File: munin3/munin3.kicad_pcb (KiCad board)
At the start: 2 copper layers, 100 x 100 mm, 83 parts, among them J1 Conn_Coaxial, J2 Conn_Coaxial, J3 Conn_01x02_Male, J4 Conn_01x02_Male, T1 Q_NMOS_DSG, T2 Q_NMOS_DSG, T3 BSS84, T4 BST82, U1 MC78L08_SO8, U2 LMC6482

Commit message: Fixed drain connection, fixed final xfmr connection
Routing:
- net Net-(C10-Pad2): track 0.00 -> 23.2 mm
- net Net-(C10-Pad1): track 0.00 -> 16.2 mm
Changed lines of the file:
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@@
     (thickness 1.6)
     (drawings 12)
-    (tracks 543)
+    (tracks 555)
     (zones 0)
     (modules 83)
@@
   (layers
     (0 F.Cu signal)
-    (31 B.Cu signal)
+    (31 B.Cu signal hide)
     (32 B.Adhes user)
     (33 F.Adhes user)
@@
   (segment (start 102.101 82.243) (end 104.6475 82.243) (width 0.4) (layer F.Cu) (net 2))
   (segment (start 104.6475 82.243) (end 104.765 82.1255) (width 0.4) (layer F.Cu) (net 2))
+  (segment (start 160.986 82.659) (end 156.008 82.659) (width 0.4) (layer F.Cu) (net 3))
+  (segment (start 156.008 82.659) (end 154.694 81.345) (width 0.4) (layer F.Cu) (net 3))
+  (segment (start 154.694 81.345) (end 147.572 81.345) (width 4) (layer F.Cu) (net 3))
+  (segment (start 147.572 81.345) (end 146.002 79.775) (width 0.4) (layer F.Cu) (net 3))
   (segment (start 106.04 127.04) (end 108.58 124.5) (width 0.4) (layer B.Cu) (net 4))
   (segment (start 105.669 88.77) (end 108.4036 86.0354) (width 0.4) (layer F.Cu) (net 4))
@@
   (segment (start 109.05 89.55) (end 109.074 89.55) (width 0.4) (layer F.Cu) (net 6))
   (via (at 109.05 89.55) (size 0.8) (drill 0.4) (layers F.Cu B.Cu) (net 6))
+  (segment (start 160.986 103.659) (end 156.54 103.659) (width 0.4) (layer F.Cu) (net 7))
+  (segment (start 156.54 103.659) (end 155.638 104.561) (width 0.4) (layer F.Cu) (net 7))
+  (segment (start 147.408 104.561) (end 146.212 105.757) (width 0.4) (layer F.Cu) (net 7))
+  (segment (start 160.986 103.659) (end 159.84 103.659) (width 0.4) (layer F.Cu) (net 7))
+  (segment (start 159.84 103.659) (end 157.263 101.082) (width 0.4) (layer F.Cu) (net 7))
+  (segment (start 157.263 101.082) (end 154.464 101.082) (width 0.4) (layer F.Cu) (net 7))
+  (segment (start 155.638 104.561) (end 150.985 104.561) (width 4) (layer F.Cu) (net 7))
+  (segment (start 150.985 104.561) (end 147.408 104.561) (width 4) (layer F.Cu) (net 7))
   (segment (start 110.609 99.675) (end 110.609 103.302) (width 0.4) (layer F.Cu) (net 8))
   (segment (start 112.455 97.823) (end 110.609 99.669) (width 0.4) (layer F.Cu) (net 8))

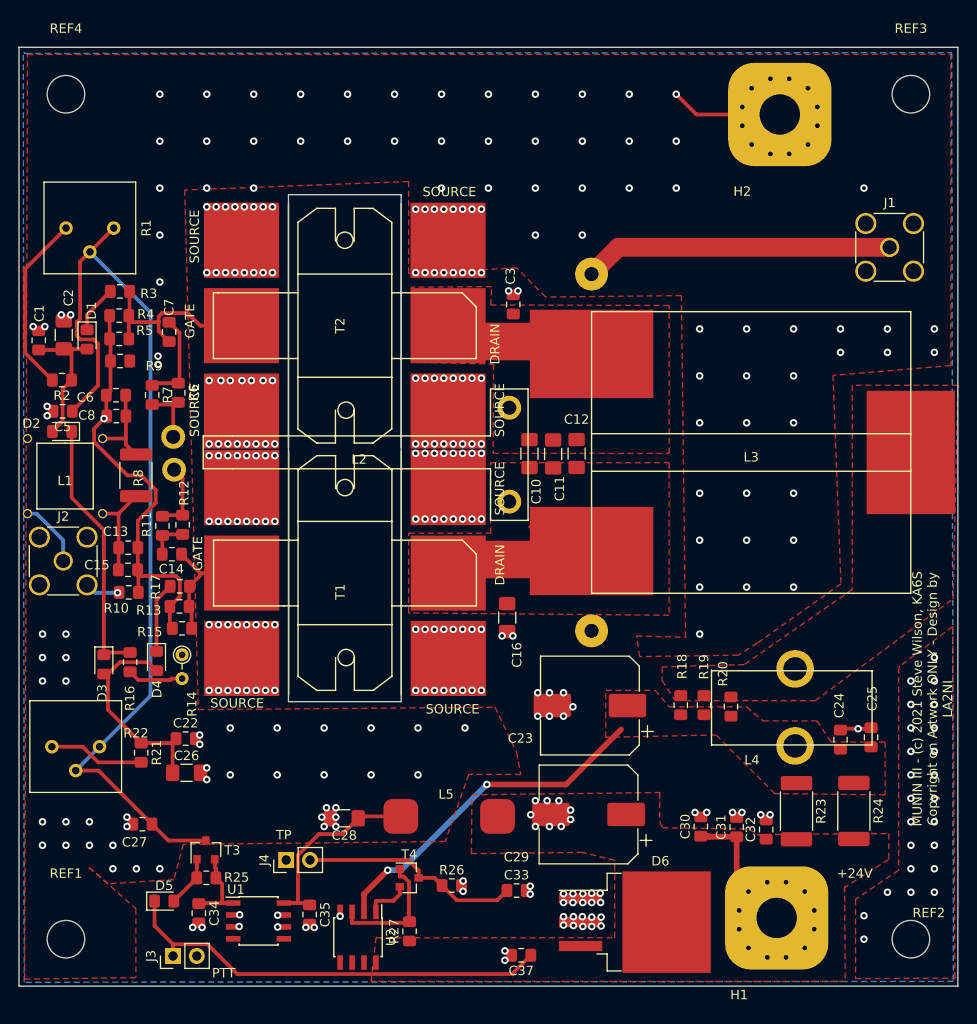
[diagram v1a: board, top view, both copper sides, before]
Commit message: Removed short between C8 and C15 on schem. Beefed up power/ground/Power Xfmr connections.
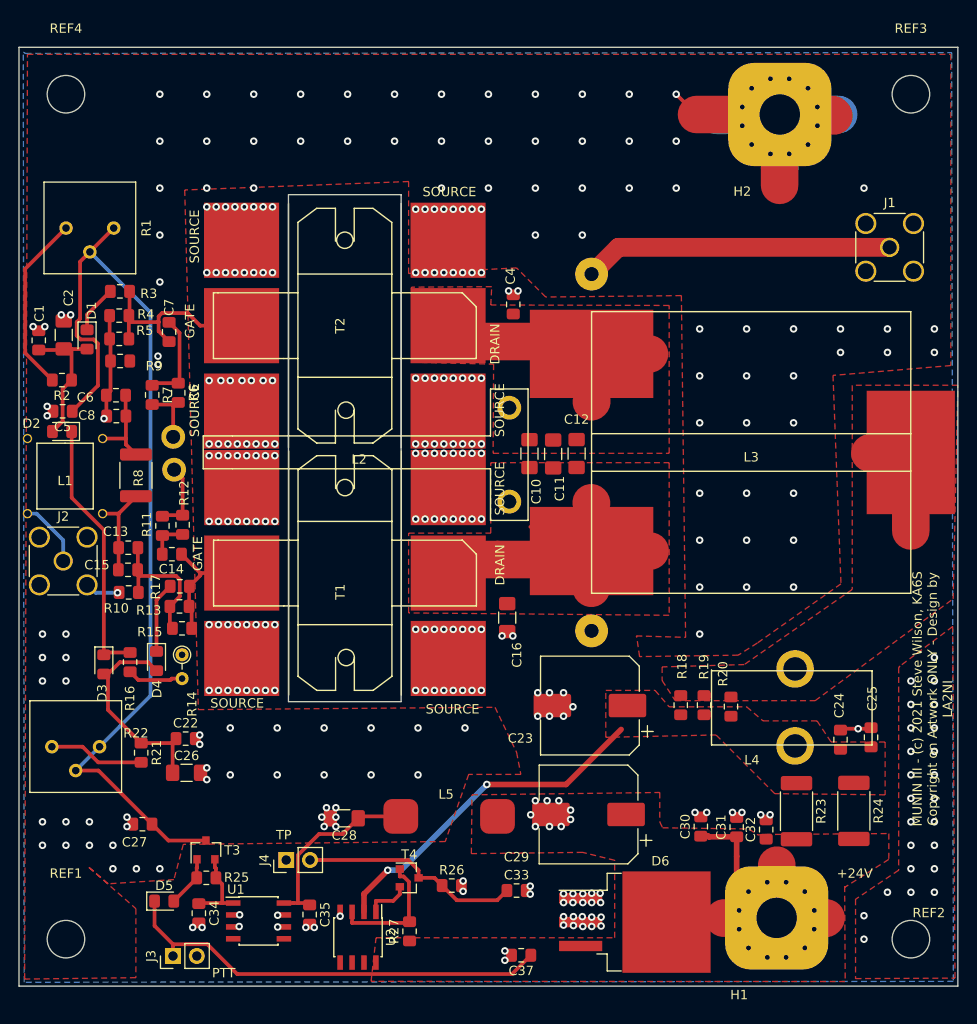
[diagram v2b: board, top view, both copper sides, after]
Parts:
- renumbered C3 to C4
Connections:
- C6 pad 1: Net-(C13-Pad1) -> Net-(C6-Pad1)
- C8 pad 1: Net-(C13-Pad1) -> Net-(C6-Pad1)
- R4 pad 1: Net-(C13-Pad1) -> Net-(C6-Pad1)
- R5 pad 1: Net-(C13-Pad1) -> Net-(C6-Pad1)
- R9 pad 1: Net-(C13-Pad1) -> Net-(C6-Pad1)
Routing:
- net GND: track 21.0 -> 61.3 mm
- net Net-(C13-Pad1): track 45.0 -> 15.1 mm, vias 1 -> 0
- net +24V: track 10.0 -> 27.6 mm
- net Net-(C10-Pad2): track 23.2 -> 40.6 mm
- net Net-(L3-Pad4): track 0.00 -> 13.5 mm
- net Net-(C10-Pad1): track 16.2 -> 28.2 mm
- net Net-(C6-Pad1): track 0.00 -> 11.3 mm, vias 0 -> 1

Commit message: Updated Version Number
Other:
- board text added: "MUNIN III - (c) 2021 Steve Wilson, KA6S v1,1 Copyright on Artwork ONLY - Design by LA2NI"
- board text removed: "MUNIN III - (c) 2021 Steve Wilson, KA6S Copyright on Artwork ONLY - Design by LA2NI"
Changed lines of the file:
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@@
   (layers
     (0 F.Cu signal)
-    (31 B.Cu signal hide)
+    (31 B.Cu signal)
     (32 B.Adhes user)
     (33 F.Adhes user)
@@
     (effects (font (size 1 1) (thickness 0.15)))
   )
-  (gr_text "MUNIN III - (c) 2021 Steve Wilson, KA6S\nCopyright on Artwork ONLY - Design by\nLA2NI" (at 197.3 119.4 90) (layer F.SilkS)
+  (gr_text "MUNIN III - (c) 2021 Steve Wilson, KA6S v1,1\nCopyright on Artwork ONLY - Design by\nLA2NI" (at 197.3 119.4 90) (layer F.SilkS)
     (effects (font (size 1 1) (thickness 0.15)))
   )
@@
   (segment (start 112.633 105.657) (end 112.659 105.631) (width 0.4) (layer F.Cu) (net 6) (status 30))
   (segment (start 112.659 105.631) (end 112.659 103.302) (width 0.4) (layer F.Cu) (net 6) (status 30))
-  (segment (start 109.649 78.582) (end 109.649 81.061) (width 0.4) (layer F.Cu) (net 36) (status 30))
-  (segment (start 109.746 83.417) (end 109.746 86.622) (width 0.4) (layer F.Cu) (net 36) (status 30))
-  (segment (start 109.746 86.622) (end 109.304 87.064) (width 0.4) (layer F.Cu) (net 36) (status 30))
-  (segment (start 109.649 81.061) (end 109.746 81.158) (width 0.4) (layer F.Cu) (net 36) (status 30))
-  (segment (start 109.746 81.158) (end 109.746 83.417) (width 0.4) (layer F.Cu) (net 36) (status 30))
   (segment (start 116.338 111.892) (end 116.067 111.621) (width 0.4) (layer F.Cu) (net 6) (status 30))
   (segment (start 116.067 111.621) (end 116.067 109.557) (width 0.4) (layer F.Cu) (net 6) (status 30))
-  (segment (start 109.338 89.286) (end 109.304 89.252) (width 0.4) (layer F.Cu) (net 36) (status 30))
-  (segment (start 109.304 89.252) (end 109.304 87.064) (width 0.4) (layer F.Cu) (net 36) (status 30))
-  (segment (start 109.074 89.55) (end 109.338 89.286) (width 0.4) (layer F.Cu) (net 36) (status 30))
-  (segment (start 109.05 89.55) (end 109.074 89.55) (width 0.4) (layer F.Cu) (net 36) (status 30))
-  (via (at 109.05 89.55) (size 0.8) (drill 0.4) (layers F.Cu B.Cu) (net 36) (status 30))
   (segment (start 160.986 103.659) (end 156.54 103.659) (width 0.4) (layer F.Cu) (net 7) (status 30))
   (segment (start 156.54 103.659) (end 155.638 104.561) (width 0.4) (layer F.Cu) (net 7) (status 30))
@@
   (segment (start 114.872 79.2728) (end 111.699 79.2728) (width 0.4) (layer F.Cu) (net 35) (status 20))
   (segment (start 123.704 79.653) (end 119.3037 79.653) (width 0.4) (layer F.Cu) (net 35) (status 10))
+  (segment (start 109.649 78.582) (end 109.649 81.061) (width 0.4) (layer F.Cu) (net 36) (status 30))
+  (segment (start 109.746 83.417) (end 109.746 86.622) (width 0.4) (layer F.Cu) (net 36) (status 30))
+  (segment (start 109.746 86.622) (end 109.304 87.064) (width 0.4) (layer F.Cu) (net 36) (status 30))
+  (segment (start 109.649 81.061) (end 109.746 81.158) (width 0.4) (layer F.Cu) (net 36) (status 30))
+  (segment (start 109.746 81.158) (end 109.746 83.417) (width 0.4) (layer F.Cu) (net 36) (status 30))
+  (segment (start 109.338 89.286) (end 109.304 89.252) (width 0.4) (layer F.Cu) (net 36) (status 30))
+  (segment (start 109.304 89.252) (end 109.304 87.064) (width 0.4) (layer F.Cu) (net 36) (status 30))
+  (segment (start 109.074 89.55) (end 109.338 89.286) (width 0.4) (layer F.Cu) (net 36) (status 30))
+  (segment (start 109.05 89.55) (end 109.074 89.55) (width 0.4) (layer F.Cu) (net 36) (status 30))
+  (via (at 109.05 89.55) (size 0.8) (drill 0.4) (layers F.Cu B.Cu) (net 36) (status 30))
   (zone (net 13) (net_name +24V) (layer F.Cu) (hatch edge 0.508)
     (connect_pads (clearance 0.508))
